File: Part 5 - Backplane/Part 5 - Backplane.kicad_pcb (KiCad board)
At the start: 2 copper layers, 154.9 x 124.5 mm, 38 parts, among them J1 BUS 1, J10 EXTENDED BUS, J11 5V DC, J2 BUS 2, J3 BUS 3, J4 BUS 4, J5 BUS 5, J6 BUS 6, J7 BUS 7, J8 BUS 8, J9 BASIC BUS, U1 LD1117AV33

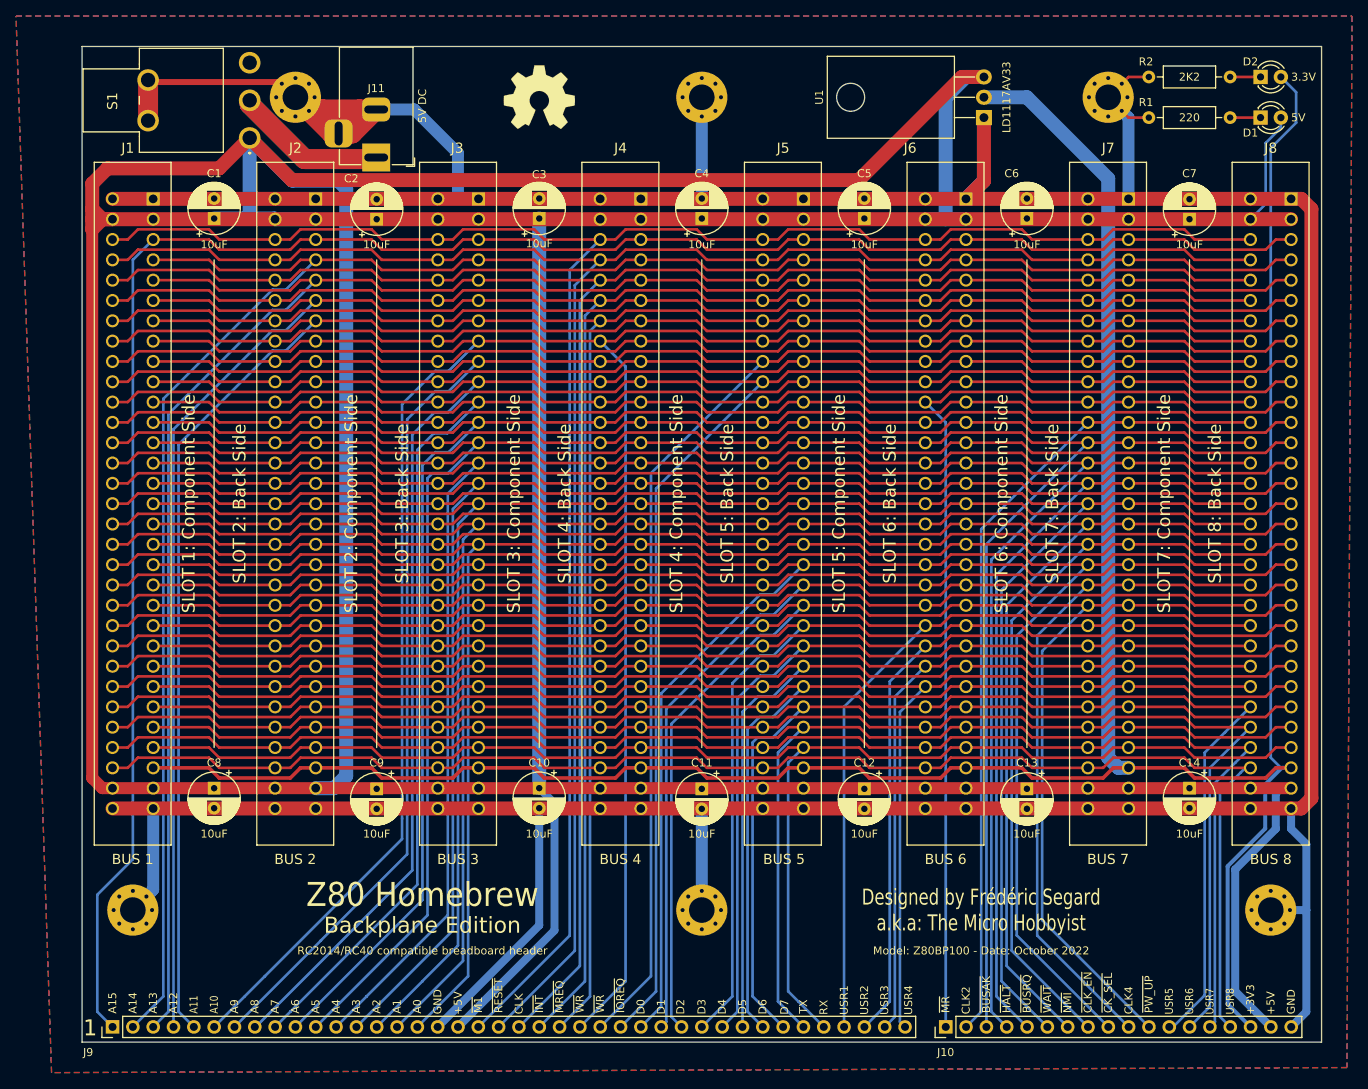
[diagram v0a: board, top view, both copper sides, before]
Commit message: Changed the clock for even cleaner clock switching
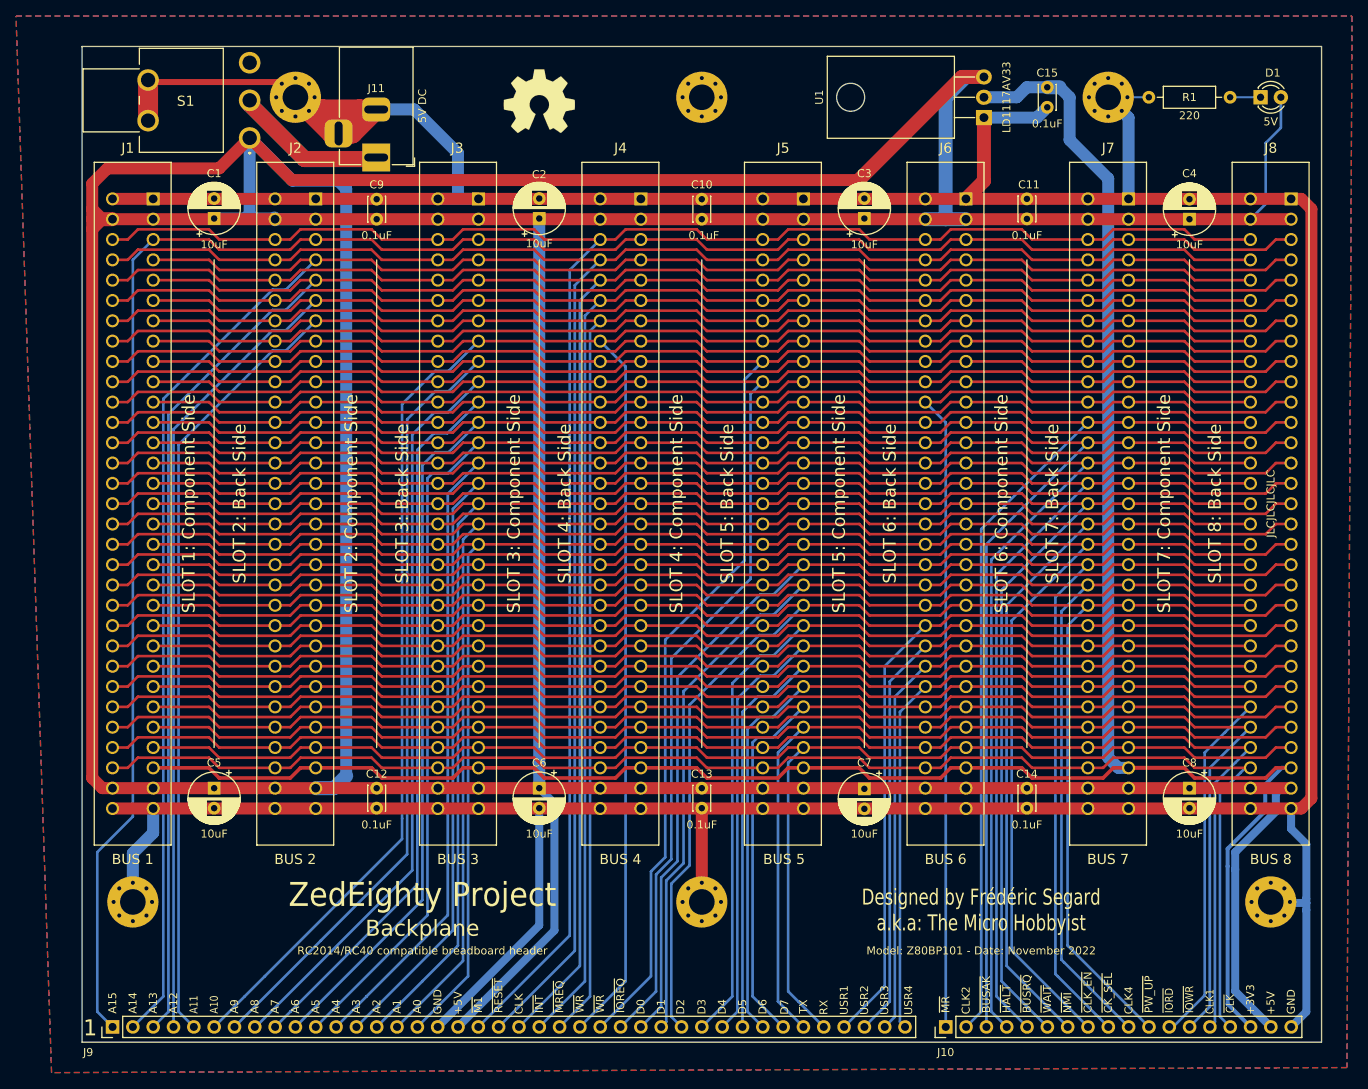
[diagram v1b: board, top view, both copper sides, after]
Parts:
- removed the C2 at (72.4, 57.1)
- removed the C4 at (113.0, 57.1)
- removed the C6 at (153.7, 57.1)
- removed D2: 3.3V, LED_THT:LED_D3.0mm
- removed R2: 2K2, Resistor_THT:R_Axial_DIN0207_L6.3mm_D2.5mm_P10.16mm_Horizontal
- removed REF**: OSHW-Symbol_8.9x8mm_SilkScreen, Symbol:OSHW-Symbol_8.9x8mm_SilkScreen
- added C10: 0.1uF, Capacitor_THT:C_Disc_D3.0mm_W2.0mm_P2.50mm, F.Cu at (113.0, 57.1)
- added C12: 0.1uF, Capacitor_THT:C_Disc_D3.0mm_W2.0mm_P2.50mm, F.Cu at (72.4, 128.3)
- added C14: 0.1uF, Capacitor_THT:C_Disc_D3.0mm_W2.0mm_P2.50mm, F.Cu at (153.7, 128.3)
- added C15: 0.1uF, Capacitor_THT:C_Disc_D3.0mm_W2.0mm_P2.50mm, F.Cu at (156.2, 40.7)
- added REF1: OSHW-Symbol_8.9x8mm_SilkScreen, Symbol:OSHW-Symbol_8.9x8mm_SilkScreen, F.Cu at (92.7, 42.4)
- C11, C13, C9: value 10uF -> 0.1uF; footprint Capacitor_THT:CP_Radial_D6.3mm_P2.50mm -> Capacitor_THT:C_Disc_D3.0mm_W2.0mm_P2.50mm
- moved C11 82.0 mm to (153.7, 57.1), turned to 90 degrees
- moved C9 71.2 mm to (72.4, 57.1), turned to 90 degrees
- moved C13 40.6 mm to (113.0, 128.3)
- moved D1 2.54 mm to (182.9, 41.9)
- moved R1 2.54 mm to (168.9, 41.9)
- moved H4 1.02 mm to (41.9, 142.5)
- moved H5 1.02 mm to (113.0, 142.5)
- moved H6 1.02 mm to (184.2, 142.5)
- renumbered C3 to C2, C5 to C3, C7 to C4, C8 to C5, C10 to C6, C12 to C7, C14 to C8
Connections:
- net /USER5 renamed /~{IORD}
- net /USER6 renamed /~{IOWR}
- net /USER7 renamed /CLK1
- net /USER8 renamed /~{CLK}
- net /~{CLK_EN} renamed /~{CLK_DIS}
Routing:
- net +3V3: track 372.6 -> 286.5 mm
- net GND: track 607.1 -> 593.8 mm
- net /~{CLK_SEL}: track 215.8 -> 211.8 mm
- net Net-(D2-Pad1): track 3.81 -> 0.00 mm
- net /~{PWR_UP}: track 210.2 -> 207.6 mm
- net +5V: track 798.9 -> 801.5 mm
- net /CLK4: track 212.2 -> 209.7 mm
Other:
- board text added: "Backplane"
- board text added: "CLK1"
- board text added: "JLCJLCJLCJLC"
- board text added: "Model: Z80BP101 - Date: November 2022"
- board text added: "ZedEighty Project"
- board text added: "~{CLK}"
- board text added: "~{IORD}"
- board text added: "~{IOWR}"
- board text removed: "Backplane Edition"
- board text removed: "Model: Z80BP100 - Date: October 2022"
- board text removed: "USR5"
- board text removed: "USR6"
- board text removed: "USR7"
- board text removed: "USR8"
- board text removed: "Z80 Homebrew"

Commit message: Added Keyboard, and minor fixes
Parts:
- removed REF1: OSHW-Symbol_8.9x8mm_SilkScreen, Symbol:OSHW-Symbol_8.9x8mm_SilkScreen
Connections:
- net /~{IORD} renamed /USER5
- net /~{IOWR} renamed /USER6
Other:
- board text added: "Designed by Frédéric Segard youtube.com/@microhobbyist"
- board text added: "Rev 2"
- board text added: "USER5"
- board text added: "USER6"
- board text removed: "Designed by Frédéric Segard a.k.a: The Micro Hobbyist"
- board text removed: "Model: Z80BP101 - Date: November 2022"
- board text removed: "~{IORD}"
- board text removed: "~{IOWR}"
